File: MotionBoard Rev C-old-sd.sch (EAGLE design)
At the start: 88 parts, among them IC1 LPC1769FBD100 or LPC4078FBD10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, IC2 LD1117, Q1 BSL207SP, Q2 12MHz, Q3 25MHz, U1 ARDUINO-FIREPICK+RAMPS, X1 ST9S008V4AR1500, X2 USB-MICRO-B

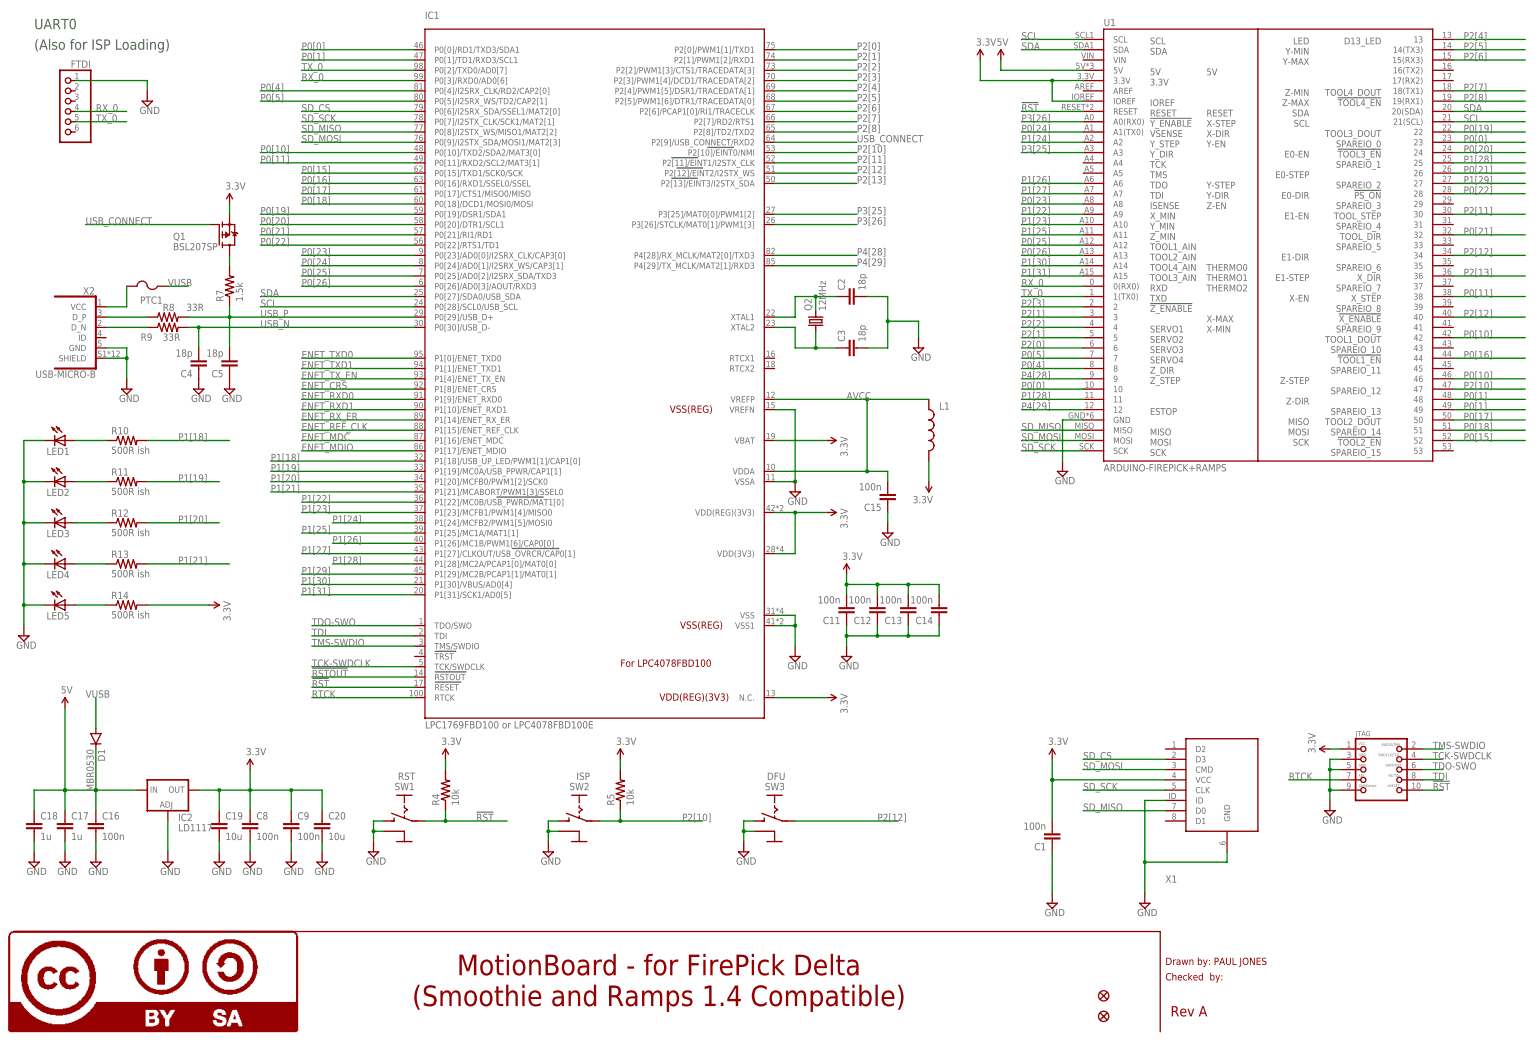
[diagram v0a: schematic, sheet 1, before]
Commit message: Update component values
Signed-off-by: Paul Jones <paul@pauljones.id.au>
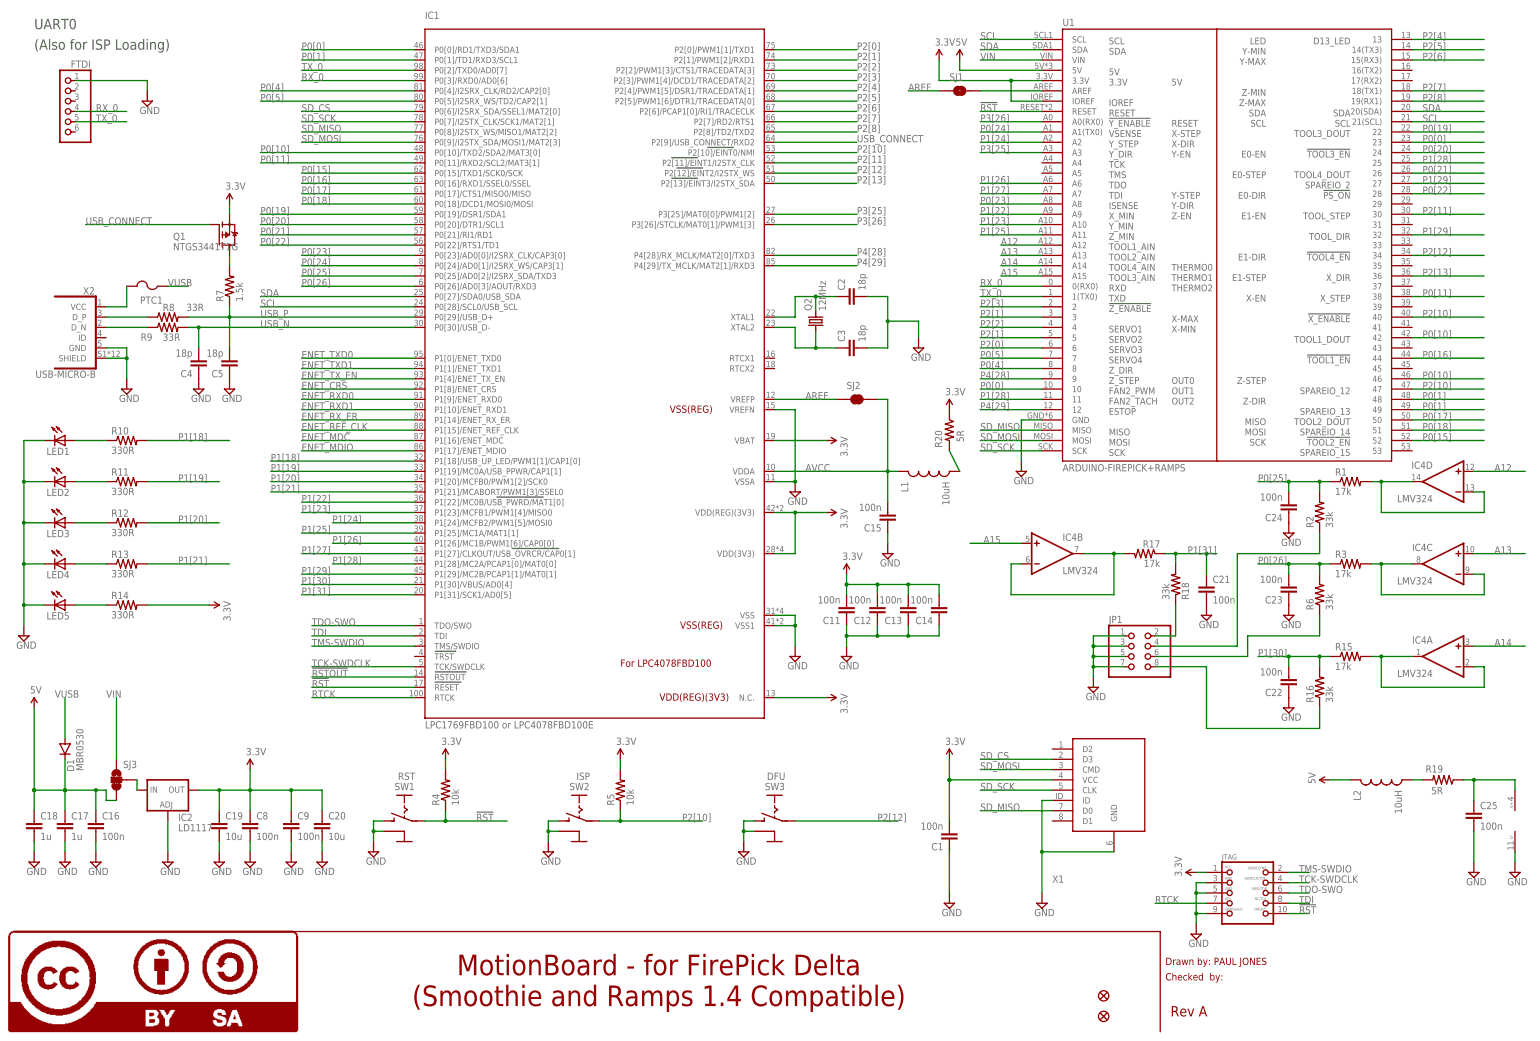
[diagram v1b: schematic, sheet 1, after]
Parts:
- removed LOGO10: LOGO-OSHWSMALL, FirePick:LOGO-OSHWSMALL
- added C21, C22, C23, C24, C25: 100n, Paul:CAP0603
- added IC4: LMV324, Paul:OPA4743UA
- added JP1: (no value), pinhead-2:PINHD-2X04_2.54-SMD
- added L2: 10uH, SparkFun:INDUCTOR0603
- added R1, R15, R17, R3: 17k, Paul:RESISTOR0603
- added R16, R18, R2, R6: 33k, Paul:RESISTOR0603
- added R19, R20: 5R, Paul:RESISTOR0603
- added SJ1: JUMPER-PAD-2-NOYES_SILK, SparkFun-Passives:JUMPER-PAD-2-NOYES_SILK
- added SJ2: JUMPER-PAD-2-NC_BY_TRACE, SparkFun-Passives:JUMPER-PAD-2-NC_BY_TRACE
- added SJ3: JUMPER-PAD-3-2OF3_NC_BY_TRACE_SMALL, SparkFun-Passives:JUMPER-PAD-3-2OF3_NC_BY_TRACE_SMALL
- C1, C10, C11, C12, C13, C14, C15, C16, C17, C18, C19, C2, C20, C3, C4, C44, C46, C5, C51, C52, C53, C54, C55, C56, C57, C58, C59, C6, C7, C8, C9: device iwt:CAP0603 -> Paul:CAP0603
- C49: value 470p -> 100n; device iwt:CAP0603 -> Paul:CAP0603
- DFU, ISP, RST: device iwt:TOGGLE-SW-SMD -> Paul:TOGGLE-SW-SMD
- IC1: device iwt:LPC1768 -> Paul:LPC1768
- L1: value (none) -> 10uH
- LED1, LED2, LED3, LED4, LED5: device iwt:LED -> Paul:LED
- Q1: value BSL207SP -> NTGS3441T1G
- R10, R11, R12, R13, R14: value 500R ish -> 330R
- R51: value 22R -> 33R
- R58, R59, R60: value 22R -> 49.9R
- RJ1: device FirePick:HR911105A -> Paul:HR911105A
- U1: device iwt:ARDUINO-FIREPICK+RAMPS -> Paul:ARDUINO-FIREPICK+RAMPS
- X2: device iwt:USB-MICRO-B -> Paul:USB-MICRO-B
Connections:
- new net A12: IC4D.+IN, U1.A12
- new net A13: IC4C.+IN, U1.A13
- new net A14: IC4A.+IN, U1.A14
- new net A15: IC4B.+IN, U1.A15
- new net AREF: IC1.VREFP, SJ1.1, SJ2.1
- new net N$10: IC4D.-IN, IC4D.OUT, R1.2
- new net N$11: JP1.8, R16.1
- new net N$13: IC4C.-IN, IC4C.OUT, R3.2
- new net N$14: JP1.6, R6.1
- new net N$16: IC4A.-IN, IC4A.OUT, R15.2
- new net N$17: JP1.4, R2.1
- new net N$18: C25.1, IC4P.V+, R19.1
- new net N$19: L2.2, R19.2
- new net N$21: L1.2, R20.2
- new net N$22: RJ1.GND
- new net N$5: SJ1.2, U1.AREF
- new net N$6: IC4B.-IN, IC4B.OUT, R17.2
- new net N$7: IC2.IN, SJ3.2
- new net N$8: JP1.2, R18.1
- new net VIN: SJ3.1, U1.VIN
- net 3.3V: now also R20.1; no longer L1.2
- net 5V: now also L2.1, SJ3.3; no longer IC2.IN
- net AVCC: now also SJ2.2; no longer IC1.VREFP
- net GND: now also C21.2, C22.1, C23.1, C24.1, C25.2, IC4P.V-, JP1.1, JP1.3, JP1.5, JP1.7; no longer RJ1.GND
- net P0[21]: no longer U1.32
- net P0[25]: now also C24.2, R1.1, R2.2; no longer U1.A12
- net P0[26]: now also C23.2, R3.1, R6.2; no longer U1.A13
- net P1[29]: now also U1.32
- net P1[30]: now also C22.2, R15.1, R16.2; no longer U1.A14
- net P1[31]: now also C21.1, R17.1, R18.2; no longer U1.A15
- net P2[10]: now also U1.40
- net P2[12]: no longer U1.40
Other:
- note added: "wire bridge"
- moved on the sheet: C1, C15, D1, JTAG, L1, X1

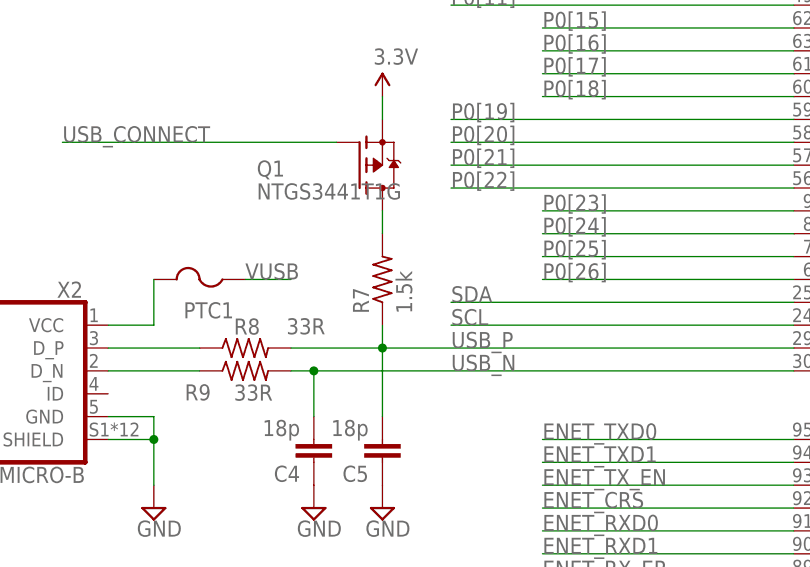
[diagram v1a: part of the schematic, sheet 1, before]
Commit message: Update component values
Signed-off-by: Paul Jones <paul@pauljones.id.au>
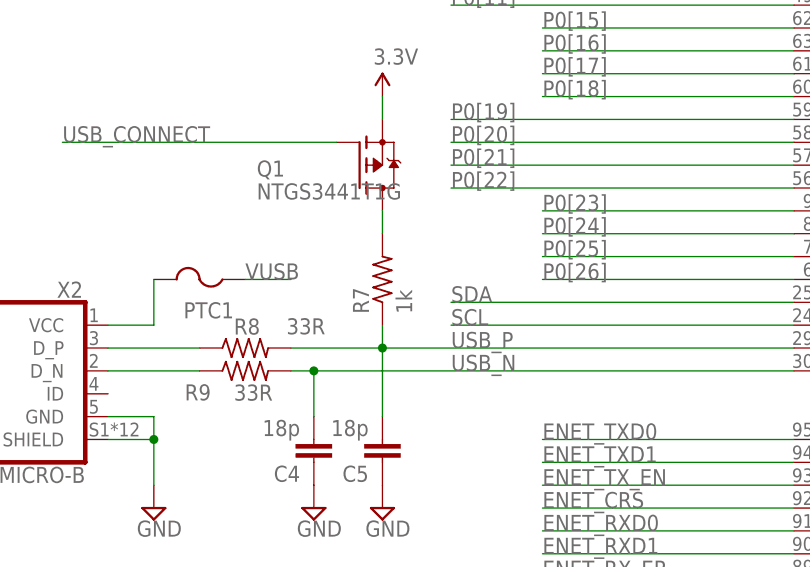
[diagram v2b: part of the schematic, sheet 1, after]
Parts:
- R52, R7: value 1.5k -> 1k
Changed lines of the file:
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@@
 <part name="P+16" library="SparkFun" deviceset="3.3V" device=""/>
 <part name="C14" library="Paul" deviceset="CAP" device="0603" value="100n"/>
-<part name="R7" library="resistor" deviceset="R-US_" device="R0603" value="1.5k"/>
+<part name="R7" library="resistor" deviceset="R-US_" device="R0603" value="1k"/>
 <part name="Q1" library="transistor-fet" deviceset="BSL207SP" device="" value="NTGS3441T1G"/>
 <part name="SUPPLY87" library="supply2" deviceset="GND" device=""/>
@@
 <part name="SUPPLY5" library="supply2" deviceset="GND" device=""/>
 <part name="IC8" library="microbuilder" deviceset="LAN8720" device=""/>
-<part name="R52" library="resistor" deviceset="R-US_" device="R0603" value="1.5k"/>
+<part name="R52" library="resistor" deviceset="R-US_" device="R0603" value="1k"/>
 <part name="R64" library="resistor" deviceset="R-US_" device="R0603" value="1M"/>
 <part name="R63" library="resistor" deviceset="R-US_" device="R0603" value="12.1k"/>
